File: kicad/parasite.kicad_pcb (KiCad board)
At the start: 2 copper layers, 22 x 110.4 mm, 30 parts, among them Q1 MMBT3904, Q2 MMBT3904, Q3 AO3407, U1 E73-2G4M08S1C-52840, U2 SHTC3, Y1 32.768kHz

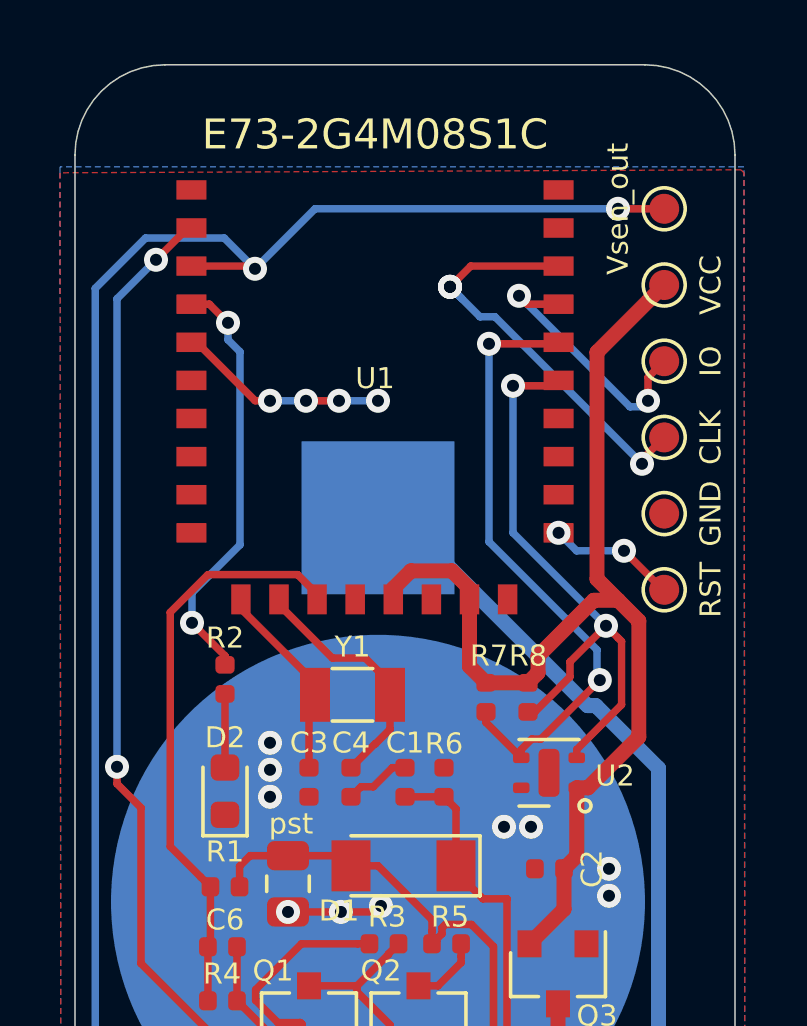
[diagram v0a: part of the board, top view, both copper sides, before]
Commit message: Add Photoresistor
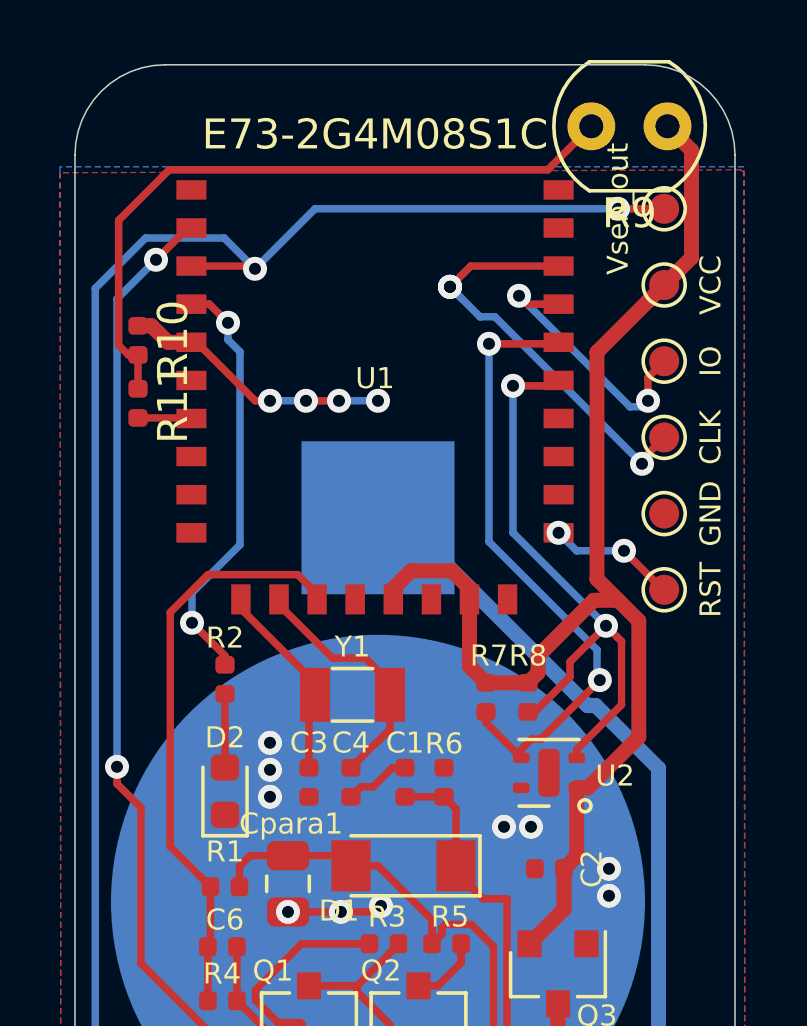
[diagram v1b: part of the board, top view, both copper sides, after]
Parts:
- added R10: 2k, Resistor_SMD:R_0402_1005Metric, F.Cu at (59.1, 36.2)
- added R11: 220, Resistor_SMD:R_0402_1005Metric, F.Cu at (59.1, 38.3)
- added R9: R_PHOTO, OptoDevice:R_LDR_4.9x4.2mm_P2.54mm_Vertical, F.Cu at (76.8, 29.1)
- renumbered pst to Cpara1
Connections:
- U1 pad 7: Net-(U1-Pad7) -> /PHOTO_OUT
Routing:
- net Net-(R10-Pad2): track 0.00 -> 23.1 mm
- net +3V0: track 37.8 -> 43.8 mm
- net GND: track 15.5 -> 17.5 mm
- net /PHOTO_OUT: track 0.00 -> 1.79 mm

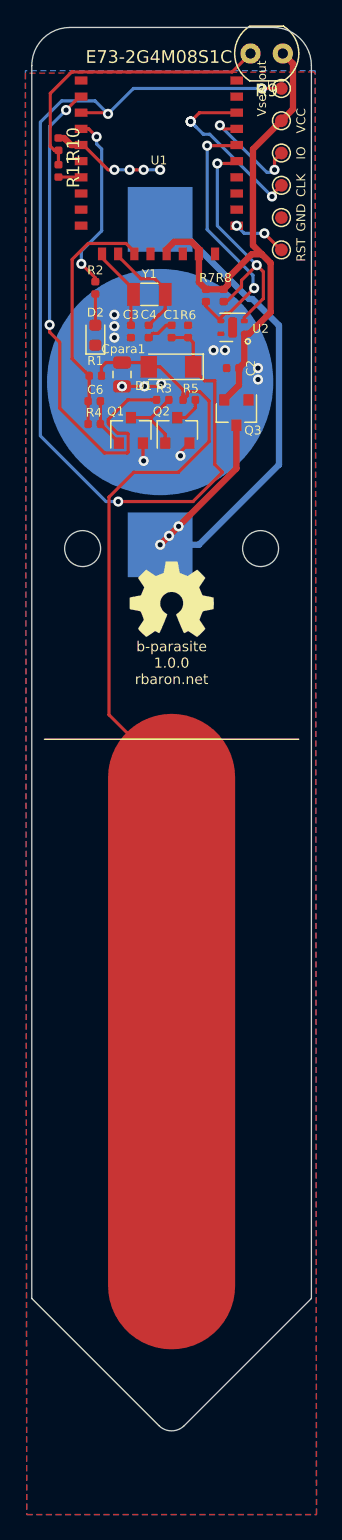
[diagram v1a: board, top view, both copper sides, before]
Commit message: Supply V to photoresitor using nrf pin
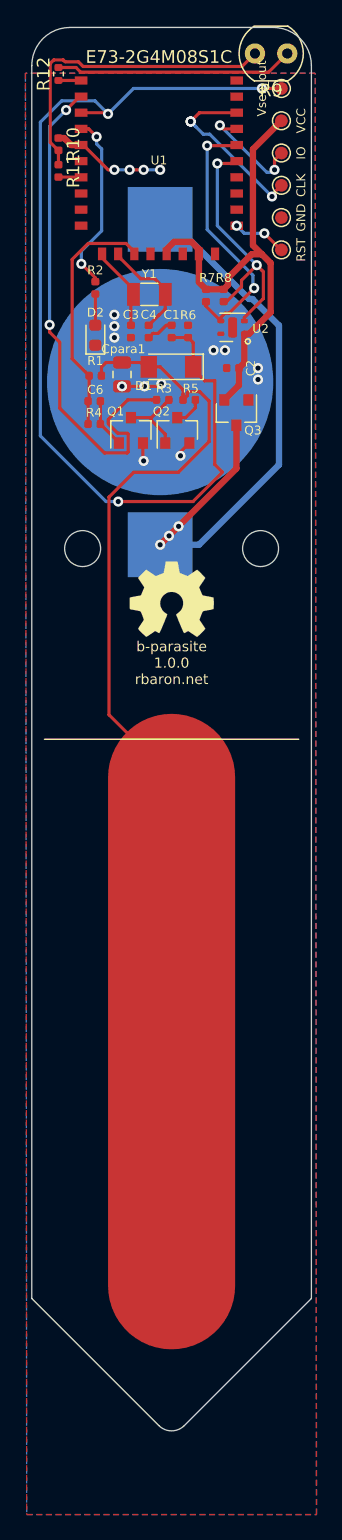
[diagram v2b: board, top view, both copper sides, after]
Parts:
- added R12: 10k, Resistor_SMD:R_0402_1005Metric, F.Cu at (59.1, 30.7)
- moved R9 0.35 mm to (77.1, 29.1)
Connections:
- R9 pad 1: +3V0 -> Net-(R12-Pad2)
- U1 pad 1: Net-(U1-Pad1) -> /PHOTO_V
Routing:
- net Net-(R12-Pad2): track 0.00 -> 18.8 mm
- net +3V0: track 43.8 -> 37.8 mm
- net Net-(R10-Pad2): track 23.1 -> 25.1 mm
- net /PHOTO_V: track 0.00 -> 1.78 mm
